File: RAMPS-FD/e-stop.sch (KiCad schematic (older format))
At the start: 11 parts, among them P302 ESTOP, U1 74HC125, U2 74HC244

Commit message: Updates to RAMPS-FD
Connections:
- net +V_LOGIC: now also R304.1; no longer R305.1
- net GND: now also R305.2; no longer R304.2
- net at D301.1 (A), U1.1 (E), U1.10 (E)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: now also P302.1 (P1), R304.2; no longer P302.2 (PM), R304.1
- net /ESTOP renamed ESTOP
- new net: P302.2 (PM), R305.1
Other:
- note added: "Emergency Stop switch (NC)\nuse jumper if not present\n\n"
- note added: "Output enable signals are active low"
- note removed: "All signals are active low"
- note removed: "To Emergency Stop switch (NC)\nuse jumper if not present\n\n"
- moved on the sheet: D301, P302, R304, R305
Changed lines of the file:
@@
-EESchema Schematic File Version 2  date 19/09/2013 22:01:21
+EESchema Schematic File Version 2
 LIBS:power
 LIBS:device
@@
 LIBS:opendous
 LIBS:RAMPS-FD-cache
-EELAYER 25  0
+EELAYER 27 0
 EELAYER END
-$Descr A4 11700 8267
+$Descr A4 11693 8268
 encoding utf-8
-Sheet 4 8
+Sheet 4 9
 Title "RAMPS-FS RAMPS for Due"
-Date "19 sep 2013"
+Date "22 sep 2013"
 Rev "0.2"
 Comp ""
@@
 F 0 "#PWR046" H 6050 3450 30  0001 C CNN
 F 1 "VCC" H 6050 3450 30  0000 C CNN
+F 2 "" H 6050 3350 60  0001 C CNN
+F 3 "" H 6050 3350 60  0001 C CNN
 	1    6050 3350
 	1    0    0    -1
@@
 	6250 3500 6250 3650
 Wire Wire Line
-	6050 3650 6050 3350
+	6050 3350 6050 3650
 Wire Wire Line
 	6150 3650 6150 3500
 Connection ~ 6050 3500
 Wire Wire Line
-	6350 3650 6350 3500
+	6350 3500 6350 3650
 Connection ~ 6250 3500
 Wire Wire Line
-	6350 3500 6050 3500
+	6050 3500 6350 3500
 Connection ~ 6150 5100
 Wire Wire Line
@@
 Connection ~ 7100 1350
 Wire Wire Line
-	7200 1500 7200 1350
-Wire Wire Line
-	7200 1350 6200 1350
+	7200 1350 7200 1500
+Wire Wire Line
+	6200 1350 7200 1350
 Connection ~ 6900 1350
 Wire Wire Line
@@
 Connection ~ 4300 6450
 Wire Wire Line
-	4300 6750 4300 5700
+	4300 5700 4300 6750
 Wire Wire Line
 	4300 5700 4450 5700
 Connection ~ 4150 5400
 Wire Wire Line
-	4850 6150 4150 6150
-Wire Wire Line
-	4150 6150 4150 3200
+	4150 6150 4850 6150
+Wire Wire Line
+	4150 3200 4150 6150
 Connection ~ 4150 4050
 Wire Wire Line
@@
 Wire Wire Line
 	4450 4350 4050 4350
-Connection ~ 4150 3200
-Wire Wire Line
-	4400 3300 4150 3300
-Connection ~ 1950 1400
+Wire Wire Line
+	1550 3300 4400 3300
 Wire Wire Line
 	3150 2900 4400 2900
@@
 	10100 900  10100 1100
 Wire Wire Line
-	1200 1400 1000 1400
-Wire Wire Line
-	2050 1200 1950 1200
-Wire Wire Line
-	1700 1400 1700 1500
-Wire Wire Line
-	7600 2700 5800 2700
+	2100 1600 2300 1600
+Wire Wire Line
+	5800 2700 7600 2700
 Wire Wire Line
 	5800 2500 7600 2500
 Wire Wire Line
-	7600 2300 5800 2300
+	5800 2300 7600 2300
 Wire Wire Line
 	3150 2800 4400 2800
@@
 	4400 2700 3150 2700
 Wire Wire Line
-	7600 2400 5800 2400
-Wire Wire Line
-	7600 2600 5800 2600
-Wire Wire Line
-	7600 2800 5800 2800
+	5800 2400 7600 2400
+Wire Wire Line
+	5800 2600 7600 2600
+Wire Wire Line
+	5800 2800 7600 2800
 Wire Wire Line
 	3150 3000 4400 3000
 Wire Wire Line
-	1700 2050 1700 2000
-Wire Wire Line
-	1950 700  1950 650
-Wire Wire Line
-	2050 1400 1600 1400
-Connection ~ 1700 1400
+	1300 2350 1300 2300
+Wire Wire Line
+	1150 1600 1700 1600
 Wire Wire Line
 	5800 2900 7600 2900
@@
 	10650 1100 10650 900
 Wire Wire Line
-	1950 1400 1950 3200
-Wire Wire Line
-	1950 3200 4400 3200
+	4150 3200 4400 3200
 Wire Wire Line
 	4050 5100 4450 5100
@@
 F 0 "#PWR047" H 6200 1300 30  0001 C CNN
 F 1 "VCC" H 6200 1300 30  0000 C CNN
+F 2 "" H 6200 1200 60  0001 C CNN
+F 3 "" H 6200 1200 60  0001 C CNN
 	1    6200 1200
 	1    0    0    -1
@@
 F 0 "RP1" H 6400 4300 40  0000 C CNN
 F 1 "R_PACK4" H 6400 3800 40  0000 C CNN
+F 2 "" H 6400 3850 60  0001 C CNN
+F 3 "" H 6400 3850 60  0001 C CNN
 	1    6400 3850
 	0    -1   -1   0
@@
 F 0 "RP3" H 7250 2150 40  0000 C CNN
 F 1 "R_PACK4" H 7250 1650 40  0000 C CNN
+F 2 "" H 7250 1700 60  0001 C CNN
+F 3 "" H 7250 1700 60  0001 C CNN
 	1    7250 1700
 	0    -1   -1   0
@@
 F 0 "RP2" H 6550 2150 40  0000 C CNN
 F 1 "R_PACK4" H 6550 1650 40  0000 C CNN
+F 2 "" H 6550 1700 60  0001 C CNN
+F 3 "" H 6550 1700 60  0001 C CNN
 	1    6550 1700
 	0    -1   -1   0
 $EndComp
 Text Notes 2000 4200 0    60   ~ 0
-All signals are active low
-Text Notes 2850 1300 0    60   ~ 0
-To Emergency Stop switch (NC)\nuse jumper if not present\n\n
+Output enable signals are active low
+Text Notes 750  650  0    60   ~ 0
+Emergency Stop switch (NC)\nuse jumper if not present\n\n
 Text GLabel 7650 5100 2    60   Output ~ 0
 /FET4_BUF
@@
 F 0 "#PWR048" H 4300 6750 30  0001 C CNN
 F 1 "GND" H 4300 6680 30  0001 C CNN
+F 2 "" H 4300 6750 60  0001 C CNN
+F 3 "" H 4300 6750 60  0001 C CNN
 	1    4300 6750
 	1    0    0    -1
@@
 F 0 "U1" H 4850 6550 50  0000 L BNN
 F 1 "74HC125" H 4900 6300 40  0000 L TNN
+F 2 "" H 4850 6450 60  0001 C CNN
+F 3 "" H 4850 6450 60  0001 C CNN
 	1    4850 6450
 	1    0    0    1
@@
 F 0 "U1" H 4900 5800 50  0000 L BNN
 F 1 "74HC125" H 4950 5550 40  0000 L TNN
+F 2 "" H 4900 5700 60  0001 C CNN
+F 3 "" H 4900 5700 60  0001 C CNN
 	4    4900 5700
 	1    0    0    1
@@
 F 0 "U1" H 4900 5200 50  0000 L BNN
 F 1 "74HC125" H 4950 4950 40  0000 L TNN
+F 2 "" H 4900 5100 60  0001 C CNN
+F 3 "" H 4900 5100 60  0001 C CNN
 	3    4900 5100
 	1    0    0    1
@@
 F 0 "U1" H 4900 4450 50  0000 L BNN
 F 1 "74HC125" H 4950 4200 40  0000 L TNN
+F 2 "" H 4900 4350 60  0001 C CNN
+F 3 "" H 4900 4350 60  0001 C CNN
 	2    4900 4350
 	1    0    0    1
@@
 F 0 "U2" H 5150 2600 60  0000 C CNN
 F 1 "74HC244" H 5200 2400 60  0000 C CNN
+F 2 "" H 5100 2800 60  0001 C CNN
+F 3 "" H 5100 2800 60  0001 C CNN
 	1    5100 2800
 	1    0    0    -1
@@
 F 0 "#PWR049" H 10650 1000 30  0001 C CNN
 F 1 "VCC" H 10650 1000 30  0000 C CNN
+F 2 "" H 10650 900 60  0001 C CNN
+F 3 "" H 10650 900 60  0001 C CNN
 	1    10650 900
 	1    0    0    -1
@@
 F 0 "#PWR050" H 10650 1700 30  0001 C CNN
 F 1 "GND" H 10650 1630 30  0001 C CNN
+F 2 "" H 10650 1700 60  0001 C CNN
+F 3 "" H 10650 1700 60  0001 C CNN
 	1    10650 1700
 	1    0    0    -1
@@
 F 0 "C2" H 10700 1400 50  0000 L CNN
 F 1 "100n" H 10700 1200 50  0000 L CNN
+F 2 "" H 10650 1300 60  0001 C CNN
+F 3 "" H 10650 1300 60  0001 C CNN
 	1    10650 1300
 	1    0    0    -1
@@
 F 0 "C1" H 10150 1400 50  0000 L CNN
 F 1 "100n" H 10150 1200 50  0000 L CNN
+F 2 "" H 10100 1300 60  0001 C CNN
+F 3 "" H 10100 1300 60  0001 C CNN
 	1    10100 1300
 	1    0    0    -1
@@
 F 0 "#PWR051" H 10100 1700 30  0001 C CNN
 F 1 "GND" H 10100 1630 30  0001 C CNN
+F 2 "" H 10100 1700 60  0001 C CNN
+F 3 "" H 10100 1700 60  0001 C CNN
 	1    10100 1700
 	1    0    0    -1
@@
 F 0 "#PWR052" H 10100 1000 30  0001 C CNN
 F 1 "VCC" H 10100 1000 30  0000 C CNN
+F 2 "" H 10100 900 60  0001 C CNN
+F 3 "" H 10100 900 60  0001 C CNN
 	1    10100 900
 	1    0    0    -1
@@
 L DIODE D301
 U 1 1 51B65AB0
-P 1400 1400
-F 0 "D301" H 1400 1500 40  0000 C CNN
-F 1 "DIODE" H 1400 1300 40  0000 C CNN
-	1    1400 1400
-	-1   0    0    1
+P 1900 1600
+F 0 "D301" H 1900 1700 40  0000 C CNN
+F 1 "DIODE" H 1900 1500 40  0000 C CNN
+F 2 "" H 1900 1600 60  0001 C CNN
+F 3 "" H 1900 1600 60  0001 C CNN
+	1    1900 1600
+	1    0    0    1
 $EndComp
 $Comp
 L R R305
 U 1 1 51B4ECD2
-P 1950 950
-F 0 "R305" V 2030 950 50  0000 C CNN
-F 1 "4k7" V 1950 950 50  0000 C CNN
-	1    1950 950
-	1    0    0    -1
+P 1300 2050
+F 0 "R305" V 1380 2050 50  0000 C CNN
+F 1 "4k7" V 1300 2050 50  0000 C CNN
+F 2 "" H 1300 2050 60  0001 C CNN
+F 3 "" H 1300 2050 60  0001 C CNN
+	1    1300 2050
+	-1   0    0    -1
 $EndComp
 $Comp
 L +V_LOGIC #PWR053
 U 1 1 51B4EC55
-P 1950 650
-F 0 "#PWR053" H 1950 620 30  0001 C CNN
-F 1 "+V_LOGIC" H 1950 750 30  0000 C CNN
-	1    1950 650
-	1    0    0    -1
+P 1550 1000
+F 0 "#PWR053" H 1550 970 30  0001 C CNN
+F 1 "+V_LOGIC" H 1550 1100 30  0000 C CNN
+F 2 "" H 1550 1000 60  0001 C CNN
+F 3 "" H 1550 1000 60  0001 C CNN
+	1    1550 1000
+	-1   0    0    -1
 $EndComp
 $Comp
 L CONN_2 P302
 U 1 1 51B4EBF7
-P 2400 1300
-F 0 "P302" V 2350 1300 40  0000 C CNN
-F 1 "ESTOP" V 2450 1300 40  0000 C CNN
-	1    2400 1300
-	1    0    0    -1
+P 800 1700
+F 0 "P302" V 750 1700 40  0000 C CNN
+F 1 "ESTOP" V 850 1700 40  0000 C CNN
+F 2 "" H 800 1700 60  0001 C CNN
+F 3 "" H 800 1700 60  0001 C CNN
+	1    800  1700
+	-1   0    0    -1
 $EndComp
 $Comp
 L R R304
 U 1 1 51B4EBD5
-P 1700 1750
-F 0 "R304" V 1780 1750 50  0000 C CNN
-F 1 "100k" V 1700 1750 50  0000 C CNN
-	1    1700 1750
-	1    0    0    -1
+P 1550 1250
+F 0 "R304" V 1630 1250 50  0000 C CNN
+F 1 "100k" V 1550 1250 50  0000 C CNN
+F 2 "" H 1550 1250 60  0001 C CNN
+F 3 "" H 1550 1250 60  0001 C CNN
+	1    1550 1250
+	-1   0    0    -1
 $EndComp
 $Comp
 L GND #PWR054
 U 1 1 51B4EBC7
-P 1700 2050
-F 0 "#PWR054" H 1700 2050 30  0001 C CNN
-F 1 "GND" H 1700 1980 30  0001 C CNN
-	1    1700 2050
-	1    0    0    -1
+P 1300 2350
+F 0 "#PWR054" H 1300 2350 30  0001 C CNN
+F 1 "GND" H 1300 2280 30  0001 C CNN
+F 2 "" H 1300 2350 60  0001 C CNN
+F 3 "" H 1300 2350 60  0001 C CNN
+	1    1300 2350
+	-1   0    0    -1
 $EndComp
 Text GLabel 7600 2300 2    60   Output ~ 0
@@
 Text GLabel 7600 2800 2    60   Output ~ 0
 /E2_EN_BUF
-Text GLabel 1000 1400 0    50   Output ~ 0
-/ESTOP
+Text GLabel 2300 1600 2    50   Output ~ 0
+ESTOP
 Text GLabel 3150 2800 0    60   Input ~ 0
 E2_EN
@@
 Text GLabel 3100 2300 0    60   Input ~ 0
 X_EN
+Wire Wire Line
+	1150 1800 1300 1800
+Wire Wire Line
+	1550 1500 1550 3300
+Connection ~ 1550 1600
 $EndSCHEMATC

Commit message: RAMPS-FD latest updates
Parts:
- D301: value DIODE -> MBR0520
- RP1, RP2, RP3: value R_PACK4 -> 10k
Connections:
- net GND: now also RP1.5 (R4), RP1.6 (R3); no longer U1.12 (D), U1.2 (D)
- net VCC: no longer RP1.5 (R4), RP1.6 (R3)
- net FET5_BUF: now reaches U1.11 (O)
- net FET5_BUF: now also RP1.3 (P3)
- net FET6_BUF: now reaches U1.3 (O)
- net FET6_BUF: now also RP1.4 (P4)
- net FET4 renamed D11-FET4
- new net D12-FET5: U1.12 (D)
- new net D2-FET6: U1.2 (D)
- no-connect marks 4 -> 0
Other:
- note added: "Active high"
- note added: "Active low"
- note added: "Or any small signal diode"
- note removed: "Output enable signals are active low"
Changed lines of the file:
@@
 Sheet 4 9
 Title "RAMPS-FS RAMPS for Due"
-Date "22 sep 2013"
+Date "23 sep 2013"
 Rev "0.2"
 Comp ""
@@
 Comment4 ""
 $EndDescr
-NoConn ~ 6350 4050
-NoConn ~ 6250 4050
-$Comp
-L VCC #PWR046
+$Comp
+L VCC #PWR047
 U 1 1 523A3BAB
 P 6050 3350
-F 0 "#PWR046" H 6050 3450 30  0001 C CNN
+F 0 "#PWR047" H 6050 3450 30  0001 C CNN
 F 1 "VCC" H 6050 3450 30  0000 C CNN
 F 2 "" H 6050 3350 60  0001 C CNN
@@
 	6350 3500 6350 3650
 Connection ~ 6250 3500
-Wire Wire Line
-	6050 3500 6350 3500
 Connection ~ 6150 5100
 Wire Wire Line
@@
 Connection ~ 4300 6450
 Wire Wire Line
-	4300 5700 4300 6750
-Wire Wire Line
-	4300 5700 4450 5700
+	4050 5700 4450 5700
 Connection ~ 4150 5400
 Wire Wire Line
@@
 Connection ~ 4150 4800
 Wire Wire Line
-	4400 6450 4300 6450
+	4050 6450 4400 6450
 Wire Wire Line
 	6200 1200 6200 1500
@@
 Connection ~ 6050 4350
 $Comp
-L VCC #PWR047
+L VCC #PWR048
 U 1 1 523A3B4A
 P 6200 1200
-F 0 "#PWR047" H 6200 1300 30  0001 C CNN
+F 0 "#PWR048" H 6200 1300 30  0001 C CNN
 F 1 "VCC" H 6200 1300 30  0000 C CNN
 F 2 "" H 6200 1200 60  0001 C CNN
@@
 P 6400 3850
 F 0 "RP1" H 6400 4300 40  0000 C CNN
-F 1 "R_PACK4" H 6400 3800 40  0000 C CNN
+F 1 "10k" H 6400 3800 40  0000 C CNN
 F 2 "" H 6400 3850 60  0001 C CNN
 F 3 "" H 6400 3850 60  0001 C CNN
@@
 P 7250 1700
 F 0 "RP3" H 7250 2150 40  0000 C CNN
-F 1 "R_PACK4" H 7250 1650 40  0000 C CNN
+F 1 "10k" H 7250 1650 40  0000 C CNN
 F 2 "" H 7250 1700 60  0001 C CNN
 F 3 "" H 7250 1700 60  0001 C CNN
@@
 P 6550 1700
 F 0 "RP2" H 6550 2150 40  0000 C CNN
-F 1 "R_PACK4" H 6550 1650 40  0000 C CNN
+F 1 "10k" H 6550 1650 40  0000 C CNN
 F 2 "" H 6550 1700 60  0001 C CNN
 F 3 "" H 6550 1700 60  0001 C CNN
@@
 	0    -1   -1   0
 $EndComp
-Text Notes 2000 4200 0    60   ~ 0
-Output enable signals are active low
 Text Notes 750  650  0    60   ~ 0
 Emergency Stop switch (NC)\nuse jumper if not present\n\n
@@
 Text GLabel 7650 4350 2    60   Output ~ 0
 /D10_BUF
-NoConn ~ 5350 5700
-NoConn ~ 5300 6450
-$Comp
-L GND #PWR048
+$Comp
+L GND #PWR049
 U 1 1 523A374A
-P 4300 6750
-F 0 "#PWR048" H 4300 6750 30  0001 C CNN
-F 1 "GND" H 4300 6680 30  0001 C CNN
-F 2 "" H 4300 6750 60  0001 C CNN
-F 3 "" H 4300 6750 60  0001 C CNN
-	1    4300 6750
+P 6650 3700
+F 0 "#PWR049" H 6650 3700 30  0001 C CNN
+F 1 "GND" H 6650 3630 30  0001 C CNN
+F 2 "" H 6650 3700 60  0001 C CNN
+F 3 "" H 6650 3700 60  0001 C CNN
+	1    6650 3700
 	1    0    0    -1
 $EndComp
 Text GLabel 4050 5100 0    60   Input ~ 0
-FET4
+D11-FET4
 Text GLabel 4050 4350 0    60   Input ~ 0
 D10
@@
 $EndComp
 $Comp
-L VCC #PWR049
+L VCC #PWR050
 U 1 1 51E4F650
 P 10650 900
-F 0 "#PWR049" H 10650 1000 30  0001 C CNN
+F 0 "#PWR050" H 10650 1000 30  0001 C CNN
 F 1 "VCC" H 10650 1000 30  0000 C CNN
 F 2 "" H 10650 900 60  0001 C CNN
@@
 $EndComp
 $Comp
-L GND #PWR050
+L GND #PWR051
 U 1 1 51E4F64F
 P 10650 1700
-F 0 "#PWR050" H 10650 1700 30  0001 C CNN
+F 0 "#PWR051" H 10650 1700 30  0001 C CNN
 F 1 "GND" H 10650 1630 30  0001 C CNN
 F 2 "" H 10650 1700 60  0001 C CNN
@@
 $EndComp
 $Comp
-L GND #PWR051
+L GND #PWR052
 U 1 1 51E4F630
 P 10100 1700
-F 0 "#PWR051" H 10100 1700 30  0001 C CNN
+F 0 "#PWR052" H 10100 1700 30  0001 C CNN
 F 1 "GND" H 10100 1630 30  0001 C CNN
 F 2 "" H 10100 1700 60  0001 C CNN
@@
 $EndComp
 $Comp
-L VCC #PWR052
+L VCC #PWR053
 U 1 1 51E4F62B
 P 10100 900
-F 0 "#PWR052" H 10100 1000 30  0001 C CNN
+F 0 "#PWR053" H 10100 1000 30  0001 C CNN
 F 1 "VCC" H 10100 1000 30  0000 C CNN
 F 2 "" H 10100 900 60  0001 C CNN
@@
 P 1900 1600
 F 0 "D301" H 1900 1700 40  0000 C CNN
-F 1 "DIODE" H 1900 1500 40  0000 C CNN
+F 1 "MBR0520" H 1900 1500 40  0000 C CNN
 F 2 "" H 1900 1600 60  0001 C CNN
 F 3 "" H 1900 1600 60  0001 C CNN
@@
 $EndComp
 $Comp
-L +V_LOGIC #PWR053
+L +V_LOGIC #PWR054
 U 1 1 51B4EC55
 P 1550 1000
-F 0 "#PWR053" H 1550 970 30  0001 C CNN
+F 0 "#PWR054" H 1550 970 30  0001 C CNN
 F 1 "+V_LOGIC" H 1550 1100 30  0000 C CNN
 F 2 "" H 1550 1000 60  0001 C CNN
@@
 $EndComp
 $Comp
-L GND #PWR054
+L GND #PWR055
 U 1 1 51B4EBC7
 P 1300 2350
-F 0 "#PWR054" H 1300 2350 30  0001 C CNN
+F 0 "#PWR055" H 1300 2350 30  0001 C CNN
 F 1 "GND" H 1300 2280 30  0001 C CNN
 F 2 "" H 1300 2350 60  0001 C CNN
@@
 	1550 1500 1550 3300
 Connection ~ 1550 1600
+Text Notes 1750 1900 0    50   ~ 0
+Or any small signal diode
+Wire Wire Line
+	6150 3500 6050 3500
+Wire Wire Line
+	6250 3500 6650 3500
+Text GLabel 4050 5700 0    50   Input ~ 0
+D12-FET5
+Wire Wire Line
+	6650 3500 6650 3700
+Text GLabel 4050 6450 0    50   Input ~ 0
+D2-FET6
+Text GLabel 7600 5700 2    50   Output ~ 0
+FET5_BUF
+Text GLabel 7600 6450 2    50   Output ~ 0
+FET6_BUF
+Wire Wire Line
+	5300 6450 7600 6450
+Wire Wire Line
+	5350 5700 7600 5700
+Wire Wire Line
+	6250 4050 6250 5700
+Connection ~ 6250 5700
+Wire Wire Line
+	6350 4050 6350 6450
+Connection ~ 6350 6450
+Wire Notes Line
+	8400 2200 8600 2200
+Wire Notes Line
+	8600 2200 8600 5300
+Wire Notes Line
+	8600 5300 8400 5300
+Wire Notes Line
+	8400 5600 8600 5600
+Wire Notes Line
+	8600 5600 8600 6550
+Wire Notes Line
+	8600 6550 8400 6550
+Text Notes 9000 3900 0    80   ~ 0
+Active low
+Text Notes 9050 6050 0    80   ~ 0
+Active high
 $EndSCHEMATC

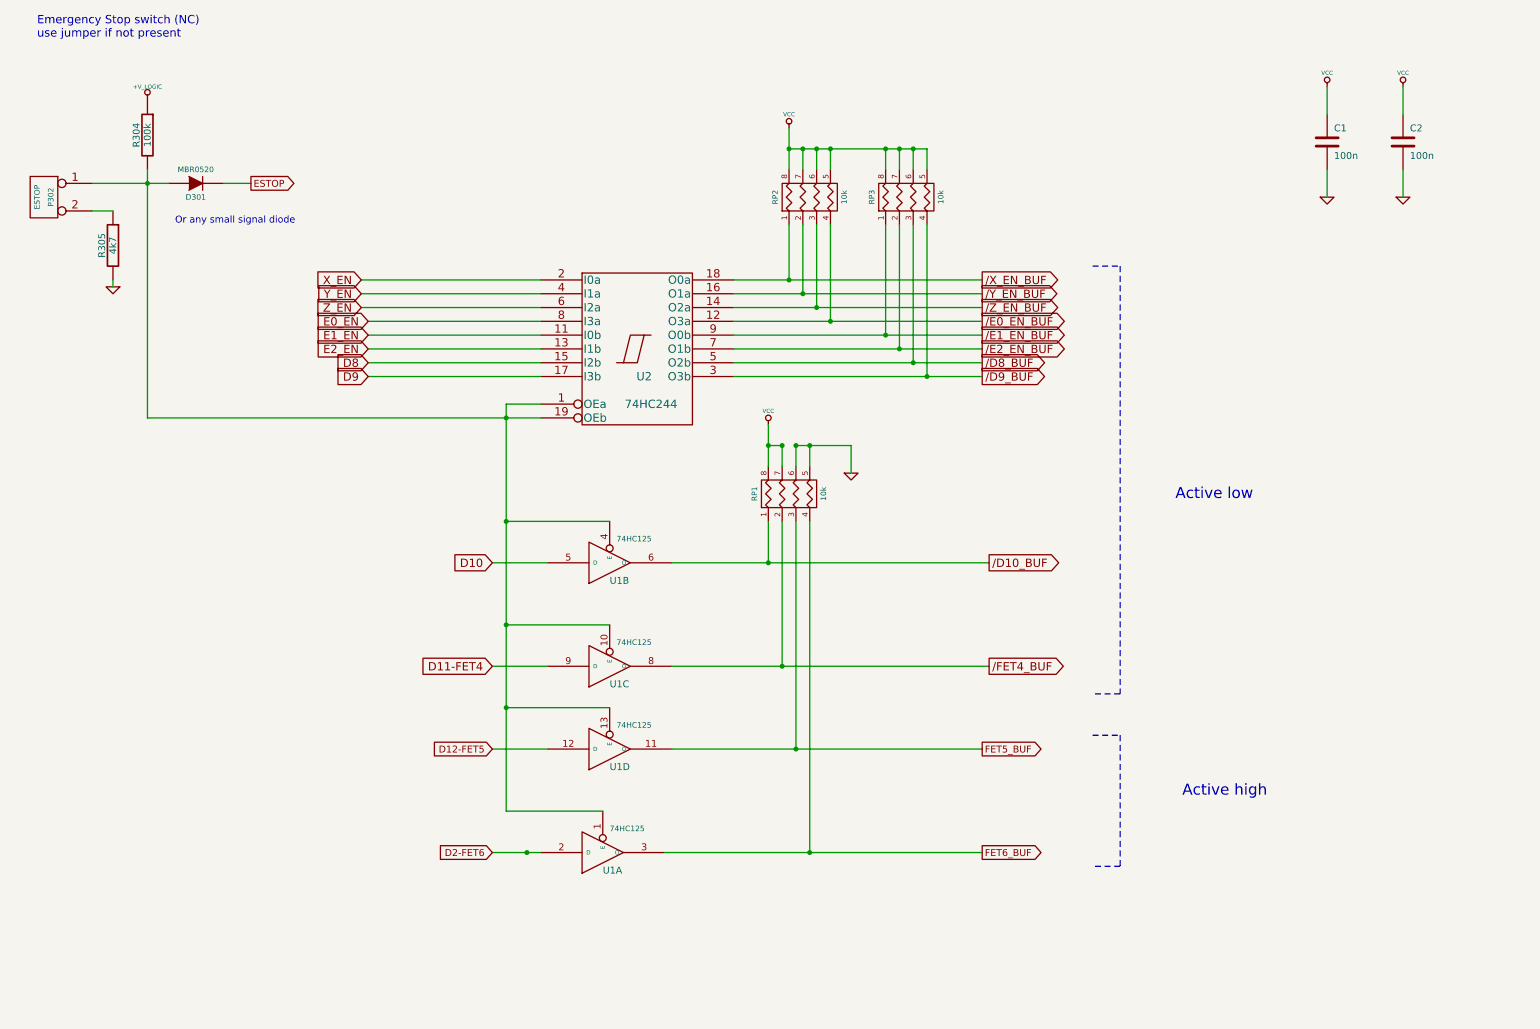
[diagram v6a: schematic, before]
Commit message: RAMPS-FD schematic changes: #3 replace C301, C302, C303 and C501 with ceramic 0805; #4 change endstop connectors to 6x1 and 6x2 to allow key position #9 change E-STOP connector to KK type; #18 add 10k pulldowns on heater outputs from CPU #19 change E-STOP buffers to HCT type to always drive FETs at 5V and remove inverting drivers on heater outputs; #20 add 24LC256 I2C EEPROM
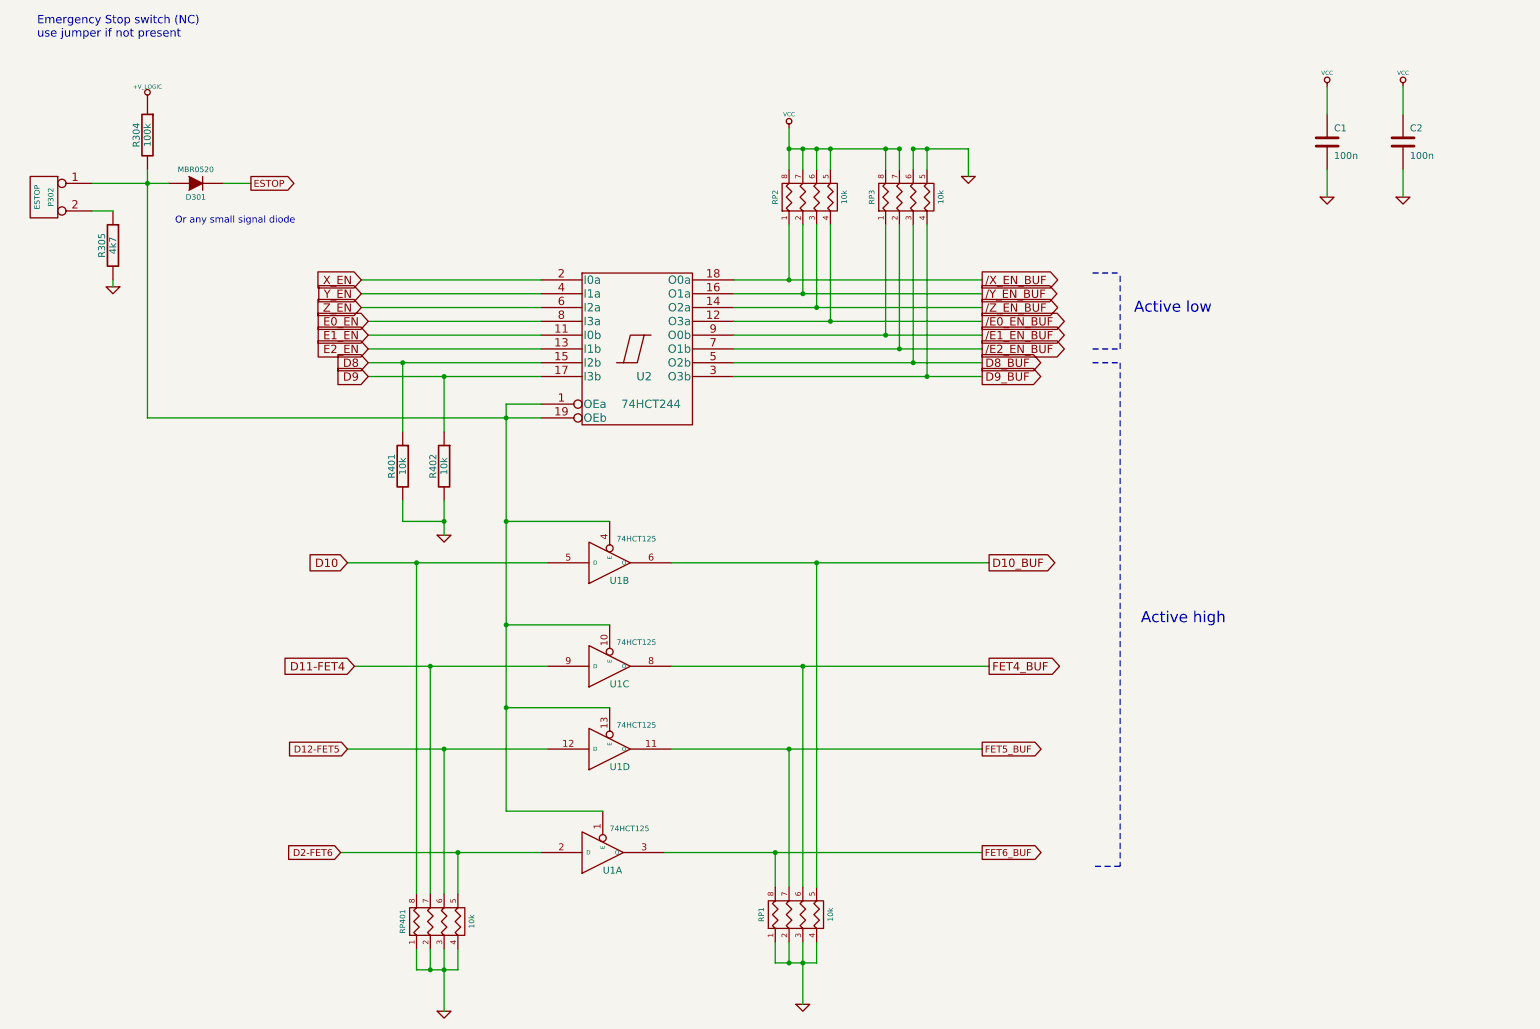
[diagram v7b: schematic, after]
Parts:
- added R401, R402: 10k, symbol R
- added RP401: 10k, symbol R_PACK4
- U1: value 74HC125 -> 74HCT125
- U2: value 74HC244 -> 74HCT244
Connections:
- net D10: now also RP401.8 (R1)
- net D11-FET4: now also RP401.7 (R2)
- net D12-FET5: now also RP401.6 (R3)
- net D2-FET6: now also RP401.5 (R4)
- net D8: now also R401.1
- net D9: now also R402.1
- net FET5_BUF: now also RP1.7 (R2); no longer RP1.3 (P3)
- net FET6_BUF: now also RP1.8 (R1); no longer RP1.4 (P4)
- net GND: now also RP1.1 (P1), RP1.2 (P2), RP1.3 (P3), RP1.4 (P4), RP3.5 (R4), RP3.6 (R3), R401.2, R402.2, RP401.1 (P1), RP401.2 (P2), RP401.3 (P3), RP401.4 (P4); no longer RP1.5 (R4), RP1.6 (R3)
- net VCC: no longer RP1.7 (R2), RP1.8 (R1), RP3.5 (R4), RP3.6 (R3)
- net /D10_BUF renamed D10_BUF
- net D10_BUF: now also RP1.5 (R4); no longer RP1.1 (P1)
- net /D8_BUF renamed D8_BUF
- net /D9_BUF renamed D9_BUF
- net /FET4_BUF renamed FET4_BUF
- net FET4_BUF: now also RP1.6 (R3); no longer RP1.2 (P2)
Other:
- moved on the sheet: RP1
